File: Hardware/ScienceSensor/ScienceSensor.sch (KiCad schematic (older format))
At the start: 12 parts

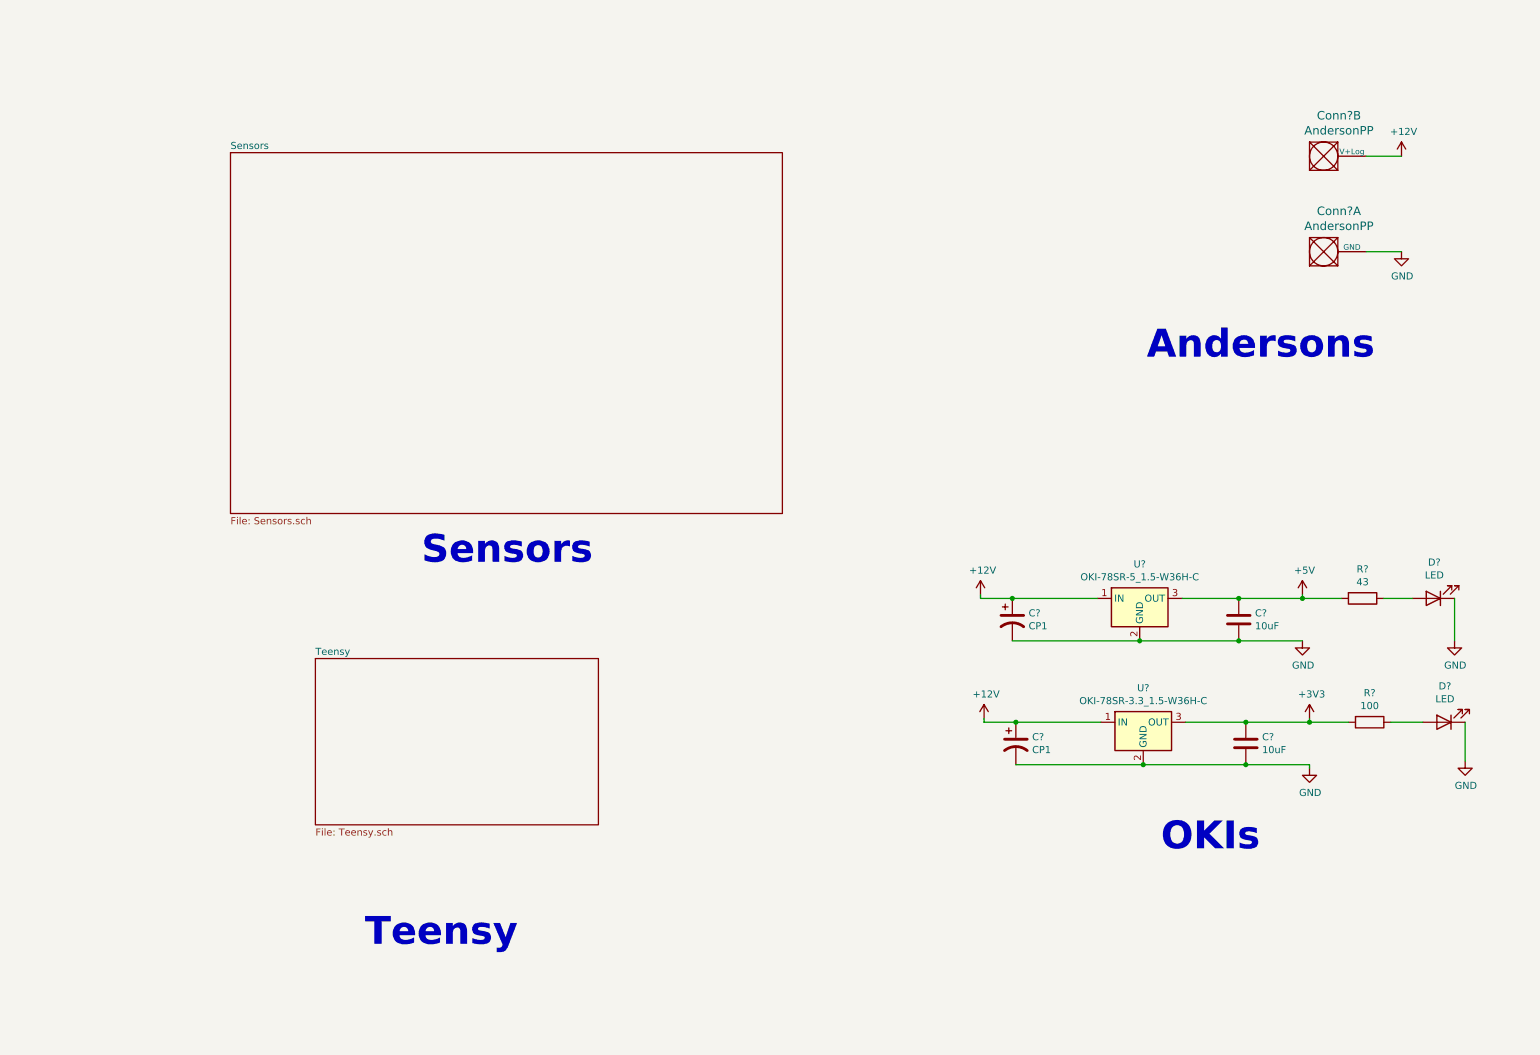
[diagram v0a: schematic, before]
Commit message: Reorganizing, added laser & photodiode sheet
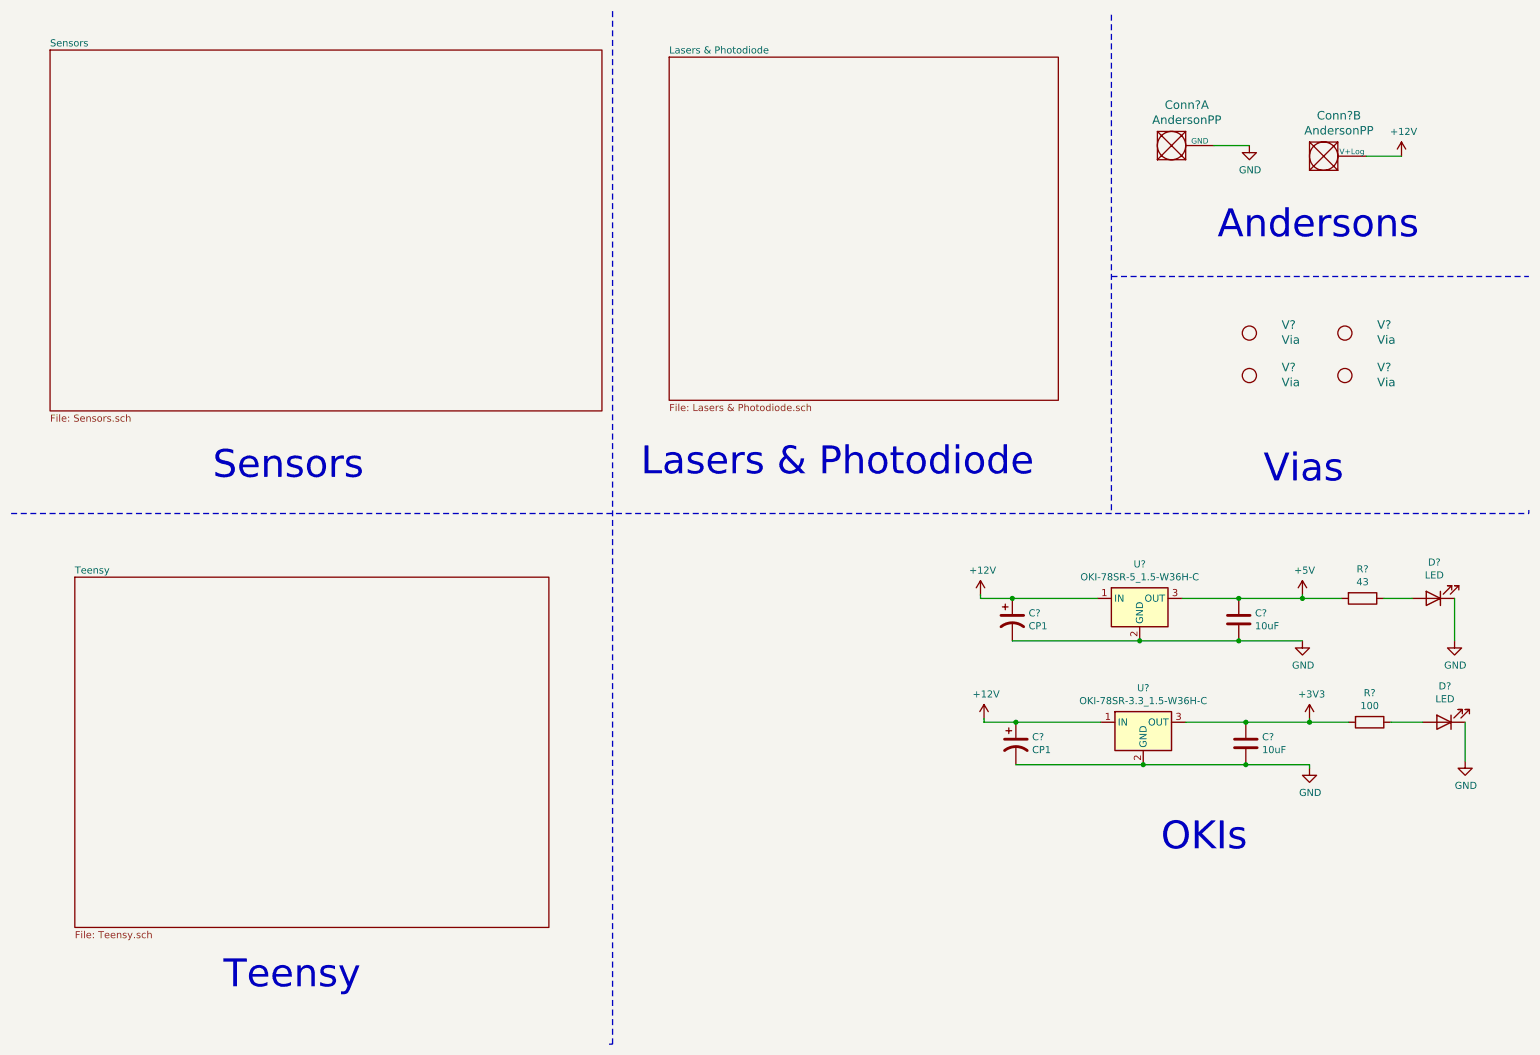
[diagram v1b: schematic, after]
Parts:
- added V? (x4): Via, symbol MRDT_Drill_Holes:Via
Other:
- note added: "Lasers & Photodiode"
- note added: "Vias"
- moved on the sheet: Conn?A
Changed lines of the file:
@@
 $Descr A4 11693 8268
 encoding utf-8
-Sheet 1 3
+Sheet 1 4
 Title ""
 Date ""
@@
 $EndDescr
 $Sheet
-S 2025 1475 3900 2550
+S 750  750  3900 2550
 U 6320EB63
 F0 "Sensors" 50
@@
 $EndSheet
 $Sheet
-S 2625 5050 2000 1175
+S 925  4475 3350 2475
 U 6320EC71
 F0 "Teensy" 50
@@
 L MRDT_Connectors:AndersonPP Conn?
 U 1 1 63213E71
-P 9650 2275
-F 0 "Conn?" H 9858 2662 60  0000 C CNN
-F 1 "AndersonPP" H 9858 2556 60  0000 C CNN
-F 2 "" H 9500 1725 60  0001 C CNN
-F 3 "" H 9500 1725 60  0001 C CNN
-	1    9650 2275
+P 8575 1525
+F 0 "Conn?" H 8783 1912 60  0000 C CNN
+F 1 "AndersonPP" H 8783 1806 60  0000 C CNN
+F 2 "" H 8425 975 60  0001 C CNN
+F 3 "" H 8425 975 60  0001 C CNN
+	1    8575 1525
 	1    0    0    -1
 $EndComp
@@
 L power:GND #PWR?
 U 1 1 6321A263
-P 10300 2175
-F 0 "#PWR?" H 10300 1925 50  0001 C CNN
-F 1 "GND" H 10305 2002 50  0000 C CNN
-F 2 "" H 10300 2175 50  0001 C CNN
-F 3 "" H 10300 2175 50  0001 C CNN
-	1    10300 2175
+P 9225 1425
+F 0 "#PWR?" H 9225 1175 50  0001 C CNN
+F 1 "GND" H 9230 1252 50  0000 C CNN
+F 2 "" H 9225 1425 50  0001 C CNN
+F 3 "" H 9225 1425 50  0001 C CNN
+	1    9225 1425
 	1    0    0    -1
 $EndComp
@@
 $EndComp
 Wire Wire Line
-	10050 2175 10300 2175
+	8975 1425 9225 1425
 Wire Wire Line
 	10300 1500 10050 1500
@@
 	-1   0    0    1
 $EndComp
-Text Notes 8600 6425 0    197  ~ 39
+Text Notes 8600 6425 0    197  ~ 0
 OKIs
-Text Notes 8500 2950 0    197  ~ 39
+Text Notes 9000 2100 0    197  ~ 0
 Andersons
-Text Notes 3375 4400 0    197  ~ 39
+Text Notes 1900 3800 0    197  ~ 0
 Sensors
-Text Notes 2975 7100 0    197  ~ 39
+Text Notes 1975 7400 0    197  ~ 0
 Teensy
+$Sheet
+S 5125 800  2750 2425
+U 63213561
+F0 "Lasers & Photodiode" 50
+F1 "Lasers & Photodiode.sch" 50
+$EndSheet
+Text Notes 4925 3775 0    197  ~ 0
+Lasers & Photodiode
+Wire Notes Line
+	8250 2350 11200 2350
+Wire Notes Line
+	8250 500  8250 4025
+Wire Notes Line
+	4725 475  4725 7775
+Wire Notes Line
+	4725 7775 4700 7775
+Wire Notes Line
+	11200 4025 11200 4000
+Wire Notes Line
+	475  4025 11200 4025
+$Comp
+L MRDT_Drill_Holes:Via V?
+U 1 1 63219785
+P 9225 2750
+F 0 "V?" H 9453 2808 60  0000 L CNN
+F 1 "Via" H 9453 2702 60  0000 L CNN
+F 2 "" H 9225 2750 60  0001 C CNN
+F 3 "" H 9225 2750 60  0001 C CNN
+	1    9225 2750
+	1    0    0    -1
+$EndComp
+$Comp
+L MRDT_Drill_Holes:Via V?
+U 1 1 6321A907
+P 9900 2750
+F 0 "V?" H 10128 2808 60  0000 L CNN
+F 1 "Via" H 10128 2702 60  0000 L CNN
+F 2 "" H 9900 2750 60  0001 C CNN
+F 3 "" H 9900 2750 60  0001 C CNN
+	1    9900 2750
+	1    0    0    -1
+$EndComp
+$Comp
+L MRDT_Drill_Holes:Via V?
+U 1 1 6321AE96
+P 9225 3050
+F 0 "V?" H 9453 3108 60  0000 L CNN
+F 1 "Via" H 9453 3002 60  0000 L CNN
+F 2 "" H 9225 3050 60  0001 C CNN
+F 3 "" H 9225 3050 60  0001 C CNN
+	1    9225 3050
+	1    0    0    -1
+$EndComp
+$Comp
+L MRDT_Drill_Holes:Via V?
+U 1 1 6321B2F5
+P 9900 3050
+F 0 "V?" H 10128 3108 60  0000 L CNN
+F 1 "Via" H 10128 3002 60  0000 L CNN
+F 2 "" H 9900 3050 60  0001 C CNN
+F 3 "" H 9900 3050 60  0001 C CNN
+	1    9900 3050
+	1    0    0    -1
+$EndComp
+Text Notes 9325 3825 0    197  ~ 0
+Vias
 $EndSCHEMATC
